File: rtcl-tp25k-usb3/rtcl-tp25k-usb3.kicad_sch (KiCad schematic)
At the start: 102 parts, among them J1 ZX360D-B-10P(30), J10 SSQ-106-02-F-D-RA, J2 0525592253, J3 BTB-DF40C-60DS-0.4V(51), J4 DF40C-60DS-0.4V(51), J5 JTAG, J6 Conn_01x02, J7 Conn_01x03, Q1 NTK3134NT1G, Q2 NTK3134NT1G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

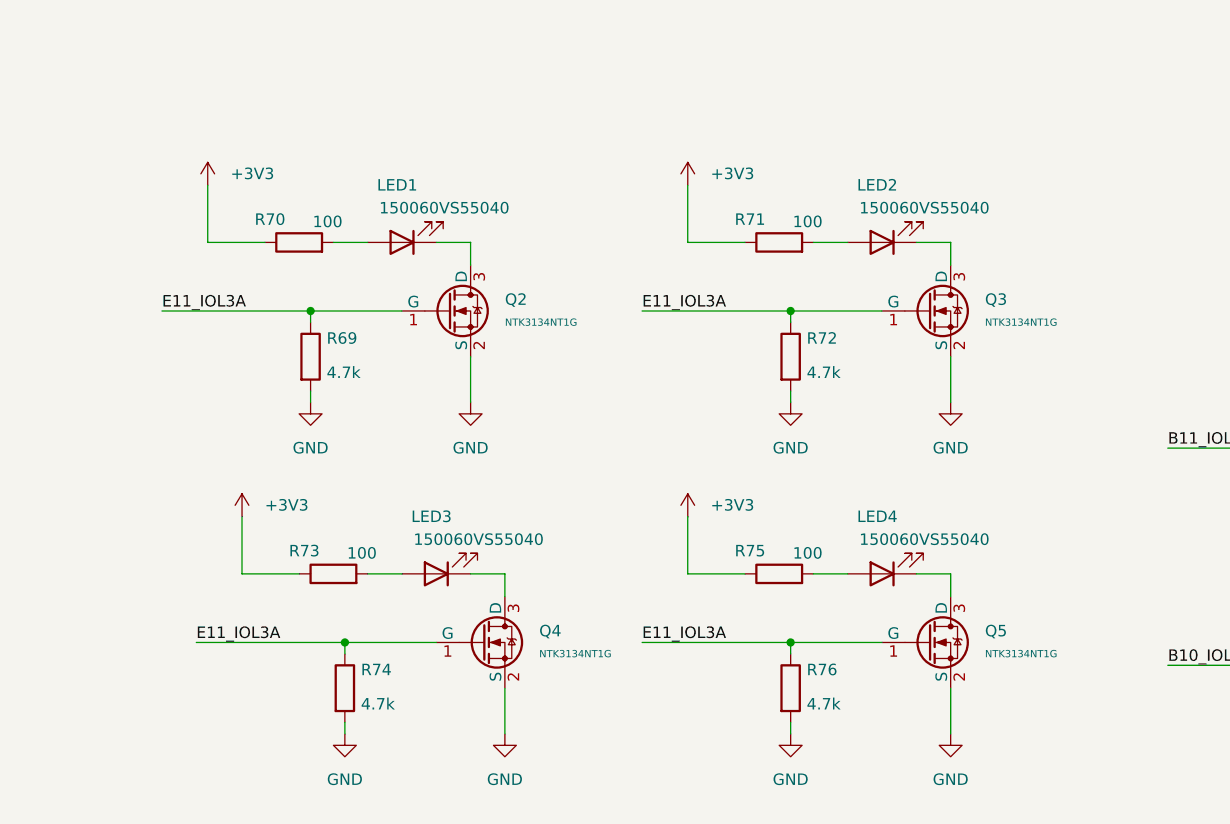
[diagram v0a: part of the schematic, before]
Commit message: Refactor KiCad project files for improved layout and organization
- Updated active layer in the project file to layer 5 for better visibility.
- Modified selection filter settings to hide dimensions, footprints, graphics, keepouts, other items, pads, tracks, vias, and zones.
- Cleared used designators in the project file to streamline component management.
- Adjusted junction and wire coordinates in the schematic for better alignment and clarity.
- Renamed labels in the schematic for consistency and clarity.
- Updated component positions and properties in the schematic to enhance layout.
- Modified footprint properties in the module file for improved design accuracy.
- Changed UUIDs for various elements to ensure uniqueness and prevent conflicts.
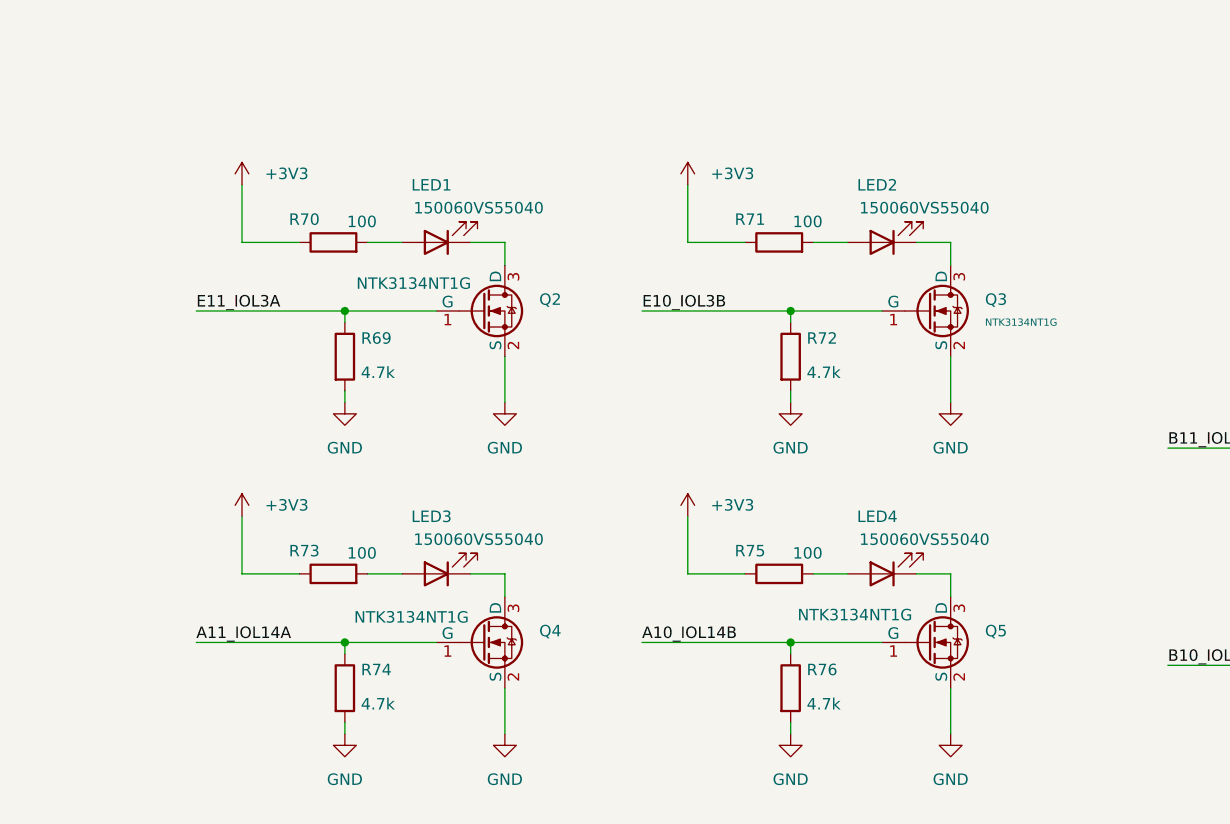
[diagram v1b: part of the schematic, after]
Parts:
- SW1, SW2, SW4: footprint (none) -> rtcl-tp25k-usb3:B3U-1100P
- SW3: footprint (none) -> rtcl-tp25k-usb3:218-2LP_CTS
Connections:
- net A10_IOL14B: now also Q5.1 (G), R76.1
- net A11_IOL14A: now also Q4.1 (G), R74.1
- net E10_IOL3B: now also Q3.1 (G), R72.1
- net E11_IOL3A: no longer Q3.1 (G), Q4.1 (G), Q5.1 (G), R72.1, R74.1, R76.1
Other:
- moved on the sheet: LED1, Q2, R69, R70

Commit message: Refactor KiCad project files: update active layer, toggle visibility settings, and remove unnecessary junctions and wires
- Changed active layer from 5 to 0 in the .kicad_prl file.
- Modified visibility settings for text, tracks, and vias in the .kicad_prl file.
- Updated visible layers string in the .kicad_prl file.
- Removed redundant junctions and wires from the .kicad_sch file to clean up the schematic.
- Added new wire connections and labels for better clarity in the .kicad_sch file.
- Adjusted positions of several labels for improved layout in the .kicad_sch file.
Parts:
- removed Q1: NTK3134NT1G, Package_TO_SOT_SMD:SOT-723, symbol PCM_JLCPCB-Transistors:NMOS,2SK3018
- removed R65: 1k, Resistor_SMD:R_0402_1005Metric, symbol Device:R
- removed R66: 4.7k, Resistor_SMD:R_0402_1005Metric, symbol Device:R
- J3: value BTB-DF40C-60DS-0.4V(51) -> DF40C(2.0)-60DS-0.4V(51)
- J4: value DF40C-60DS-0.4V(51) -> DF40C(2.0)-60DS-0.4V(51)
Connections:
- net MIPI_GPIO0 is gone; now on net A1_IOB24A_40P: J2.17 (GPIO0)
- net MIPI_GPIO1 is gone; now on net E3_IOB60A_40P: J2.18 (GPIO1)
- net A10_IOL14B: now also Q2.1 (G), R69.1; no longer Q5.1 (G), R76.1
- net A11_IOL14A: now also Q3.1 (G), R72.1; no longer Q4.1 (G), R74.1
- net B10_IOL12B: now also C11.2, R78.1; no longer C12.2, R79.1
- net B11_IOL12A: now also C12.2, R79.1; no longer C11.2, R78.1
- net E10_IOL3B: now also Q4.1 (G), R74.1; no longer Q3.1 (G), R72.1
- net E11_IOL3A: now also Q5.1 (G), R76.1; no longer Q2.1 (G), R69.1

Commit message: WIP
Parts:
- J10: footprint rtcl-p25k-usb3:PMOD_02x06_2.54mm -> rtcl-tp25k-usb3:PMOD_02x06_2.54mm
- J4: footprint rtcl-p25k-usb3:CONN_DF40C-60DS_HIR -> rtcl-tp25k-usb3:CONN_DF40C-60DS_HIR
- L1: footprint rtcl-p25k-usb3:INDC2016X100N -> rtcl-tp25k-usb3:INDC2016X100N
- RN1, RN2, RN3, RN4, RN5, RN6, RN7, RN8, RN9: footprint rtcl-p25k-usb3:RES_YC104_YAG -> rtcl-tp25k-usb3:RES_YC104_YAG
- U4: footprint rtcl-p25k-usb3:DMQ0006A -> rtcl-tp25k-usb3:DMQ0006A
- X1: footprint rtcl-p25k-usb3:XTAL_ABM8-30.000MHz-D1X-T -> rtcl-tp25k-usb3:XTAL_ABM8-30.000MHz-D1X-T
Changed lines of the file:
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@@
 			)
 		)
-		(property "Footprint" "rtcl-p25k-usb3:RES_YC104_YAG"
+		(property "Footprint" "rtcl-tp25k-usb3:RES_YC104_YAG"
 			(at 251.46 203.835 90)
 			(hide yes)
@@
 			)
 		)
-		(property "Footprint" "rtcl-p25k-usb3:RES_YC104_YAG"
+		(property "Footprint" "rtcl-tp25k-usb3:RES_YC104_YAG"
 			(at 251.46 306.705 90)
 			(hide yes)
@@
 			)
 		)
-		(property "Footprint" "rtcl-p25k-usb3:DMQ0006A"
+		(property "Footprint" "rtcl-tp25k-usb3:DMQ0006A"
 			(at 97.79 525.526 0)
 			(hide yes)
@@
 			)
 		)
-		(property "Footprint" "rtcl-p25k-usb3:RES_YC104_YAG"
+		(property "Footprint" "rtcl-tp25k-usb3:RES_YC104_YAG"
 			(at 251.46 276.225 90)
 			(hide yes)
@@
 			)
 		)
-		(property "Footprint" "rtcl-p25k-usb3:RES_YC104_YAG"
+		(property "Footprint" "rtcl-tp25k-usb3:RES_YC104_YAG"
 			(at 251.46 342.265 90)
 			(hide yes)
@@
 			)
 		)
-		(property "Footprint" "rtcl-p25k-usb3:CONN_DF40C-60DS_HIR"
+		(property "Footprint" "rtcl-tp25k-usb3:CONN_DF40C-60DS_HIR"
 			(at 486.41 278.13 0)
 			(hide yes)
@@
 			)
 		)
-		(property "Footprint" "rtcl-p25k-usb3:RES_YC104_YAG"
+		(property "Footprint" "rtcl-tp25k-usb3:RES_YC104_YAG"
 			(at 251.46 250.825 90)
 			(hide yes)
@@
 			)
 		)
-		(property "Footprint" "rtcl-p25k-usb3:RES_YC104_YAG"
+		(property "Footprint" "rtcl-tp25k-usb3:RES_YC104_YAG"
 			(at 251.46 286.385 90)
 			(hide yes)
@@
 			)
 		)
-		(property "Footprint" "rtcl-p25k-usb3:XTAL_ABM8-30.000MHz-D1X-T"
+		(property "Footprint" "rtcl-tp25k-usb3:XTAL_ABM8-30.000MHz-D1X-T"
 			(at 134.62 311.15 0)
 			(hide yes)
@@
 			)
 		)
-		(property "Footprint" "rtcl-p25k-usb3:RES_YC104_YAG"
+		(property "Footprint" "rtcl-tp25k-usb3:RES_YC104_YAG"
 			(at 251.46 316.865 90)
 			(hide yes)
@@
 			)
 		)
-		(property "Footprint" "rtcl-p25k-usb3:RES_YC104_YAG"
+		(property "Footprint" "rtcl-tp25k-usb3:RES_YC104_YAG"
 			(at 251.46 332.105 90)
 			(hide yes)
@@
 			)
 		)
-		(property "Footprint" "rtcl-p25k-usb3:RES_YC104_YAG"
+		(property "Footprint" "rtcl-tp25k-usb3:RES_YC104_YAG"
 			(at 251.46 260.985 90)
 			(hide yes)
@@
 			)
 		)
-		(property "Footprint" "rtcl-p25k-usb3:INDC2016X100N"
+		(property "Footprint" "rtcl-tp25k-usb3:INDC2016X100N"
 			(at 125.73 502.92 0)
 			(hide yes)
@@
 			)
 		)
-		(property "Footprint" "rtcl-p25k-usb3:PMOD_02x06_2.54mm"
+		(property "Footprint" "rtcl-tp25k-usb3:PMOD_02x06_2.54mm"
 			(at 488.95 415.29 0)
 			(hide yes)

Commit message: DRCは通した
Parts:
- J1: footprint rtcl-p25k-usb3:CONN10_ZX360D-B-10P30_HIR -> rtcl-tp25k-usb3:CONN10_ZX360D-B-10P30_HIR
- J2: footprint rtcl-p25k-usb3:CON_525592253_MOL -> rtcl-tp25k-usb3:CON_525592253_MOL
- J3: footprint rtcl-p25k-usb3:CONN_DF40C-60DS_HIR -> rtcl-tp25k-usb3:CONN_DF40C-60DS_HIR
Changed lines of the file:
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@@
 			)
 		)
-		(property "Footprint" "rtcl-p25k-usb3:CON_525592253_MOL"
+		(property "Footprint" "rtcl-tp25k-usb3:CON_525592253_MOL"
 			(at 176.784 390.652 0)
 			(hide yes)
@@
 			)
 		)
-		(property "Footprint" "rtcl-p25k-usb3:CONN_DF40C-60DS_HIR"
+		(property "Footprint" "rtcl-tp25k-usb3:CONN_DF40C-60DS_HIR"
 			(at 383.54 278.13 0)
 			(hide yes)
@@
 			)
 		)
-		(property "Footprint" "rtcl-p25k-usb3:CONN10_ZX360D-B-10P30_HIR"
+		(property "Footprint" "rtcl-tp25k-usb3:CONN10_ZX360D-B-10P30_HIR"
 			(at 52.07 186.69 0)
 			(hide yes)

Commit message: PMOD配線長調整
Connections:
- net VCCIO33 is gone; now on net +3V3: C77.1, J10.11 (Pin_11), J10.12 (Pin_12)
- no-connect marks 0 -> 1
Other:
- moved on the sheet: C1, C10, C11, C12, C15, C16, C17, C18, C19, C2, C20, C21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

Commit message: WIP
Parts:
- added R81: 4.7k, Resistor_SMD:R_0402_1005Metric, symbol Device:R
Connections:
- net A1_IOB24A_40P: now also R81.1
- net GND: now also R81.2
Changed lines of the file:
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@@
 	)
 	(junction
+		(at 337.82 86.36)
+		(diameter 0)
+		(color 0 0 0 0)
+	)
+	(junction
 		(at 279.4 80.01)
 		(diameter 0)
@@
 	(wire
 		(pts
-			(xy 339.09 86.36) (xy 339.09 69.85)
+			(xy 342.9 86.36) (xy 342.9 69.85)
 		)
 		(stroke
@@
 	(wire
 		(pts
+			(xy 337.82 99.06) (xy 337.82 100.33)
+		)
+		(stroke
+			(width 0)
+			(type default)
+		)
+	)
+	(wire
+		(pts
 			(xy 82.55 240.03) (xy 82.55 241.3)
 		)
@@
 	(wire
 		(pts
+			(xy 337.82 86.36) (xy 337.82 91.44)
+		)
+		(stroke
+			(width 0)
+			(type default)
+		)
+	)
+	(wire
+		(pts
 			(xy 217.17 111.76) (xy 194.31 111.76)
 		)
@@
 	(wire
 		(pts
-			(xy 321.31 88.9) (xy 341.63 88.9)
+			(xy 321.31 88.9) (xy 345.44 88.9)
 		)
 		(stroke
@@
 	(wire
 		(pts
+			(xy 337.82 86.36) (xy 342.9 86.36)
+		)
+		(stroke
+			(width 0)
+			(type default)
+		)
+	)
+	(wire
+		(pts
 			(xy 288.29 80.01) (xy 279.4 80.01)
 		)
@@
 	(wire
 		(pts
-			(xy 341.63 72.39) (xy 372.11 72.39)
+			(xy 345.44 72.39) (xy 372.11 72.39)
 		)
 		(stroke
@@
 	(wire
 		(pts
-			(xy 339.09 69.85) (xy 372.11 69.85)
+			(xy 342.9 69.85) (xy 372.11 69.85)
 		)
 		(stroke
@@
 	(wire
 		(pts
-			(xy 321.31 86.36) (xy 339.09 86.36)
+			(xy 321.31 86.36) (xy 337.82 86.36)
 		)
 		(stroke
@@
 	(wire
 		(pts
-			(xy 341.63 72.39) (xy 341.63 88.9)
+			(xy 345.44 72.39) (xy 345.44 88.9)
 		)
 		(stroke
@@
 	)
 	(symbol
+		(lib_id "Device:R")
+		(at 337.82 95.25 0)
+		(unit 1)
+		(body_style 1)
+		(exclude_from_sim no)
+		(in_bom yes)
+		(on_board yes)
+		(in_pos_files yes)
+		(dnp no)
+		(property "Reference" "R81"
+			(at 339.598 93.218 0)
+			(show_name no)
+			(do_not_autoplace no)
+			(effects
+				(font
+					(size 1.27 1.27)
+				)
+				(justify left)
+			)
+		)
+		(property "Value" "4.7k"
+			(at 339.598 97.028 0)
+			(show_name no)
+			(do_not_autoplace no)
+			(effects
+				(font
+					(size 1.27 1.27)
+				)
+				(justify left)
+			)
+		)
+		(property "Footprint" "Resistor_SMD:R_0402_1005Metric"
+			(at 336.042 95.25 90)
+			(hide yes)
+			(show_name no)
+			(do_not_autoplace no)
+			(effects
+				(font
+					(size 1.27 1.27)
+				)
+			)
+		)
+		(property "Datasheet" ""
+			(at 337.82 95.25 0)
+			(hide yes)
+			(show_name no)
+			(do_not_autoplace no)
+			(effects
+				(font
+					(size 1.27 1.27)
+				)
+			)
+		)
+		(property "Description" "Resistor"
+			(at 337.82 95.25 0)
+			(hide yes)
+			(show_name no)
+			(do_not_autoplace no)
+			(effects
+				(font
+					(size 1.27 1.27)
+				)
+			)
+		)
+		(pin "1"
+		)
+		(pin "2"
+		)
+		(instances
+			(project "rtcl-tp25k-usb3"
+				(path "/3111823c-3b86-4a35-a2d4-382a0824eec6"
+					(reference "R81")
+					(unit 1)
+				)
+			)
+		)
+	)
+	(symbol
 		(lib_id "Device:R_Pack04")
 		(at 189.23 137.16 270)
@@
 					(unit 1)
 				)
+			)
+		)
+	)
+	(symbol
+		(lib_id "power:GND")
+		(at 337.82 100.33 0)
+		(unit 1)
+		(body_style 1)
+		(exclude_from_sim no)
+		(in_bom yes)
+		(on_board yes)
+		(in_pos_files yes)
+		(dnp no)
+		(property "Reference" "#PWR0111"
+			(at 337.82 106.68 0)
+			(hide yes)
+			(show_name no)
+			(do_not_autoplace no)
+			(effects
+				(font
+					(size 1.27 1.27)
+				)
+			)
+		)
+		(property "Value" "GND"
+			(at 341.63 102.362 0)
+			(show_name no)
+			(do_not_autoplace no)
+			(effects
+				(font
+					(size 1.27 1.27)
+				)
+			)
+		)
+		(property "Footprint" ""
+			(at 337.82 100.33 0)
+			(hide yes)
+			(show_name no)
+			(do_not_autoplace no)
+			(effects
+				(font
+					(size 1.27 1.27)
+				)
+			)
+		)
+		(property "Datasheet" ""
+			(at 337.82 100.33 0)
+			(hide yes)
+			(show_name no)
+			(do_not_autoplace no)
+			(effects
+				(font
+					(size 1.27 1.27)
+				)
+			)
+		)
+		(property "Description" "Power symbol creates a global label with name \"GND\" , ground"
+			(at 337.82 100.33 0)
+			(hide yes)
+			(show_name no)
+			(do_not_autoplace no)
+			(effects
+				(font
+					(size 1.27 1.27)
+				)
+			)
+		)
+		(pin "1"
+		)
+		(instances
+			(project "rtcl-tp25k-usb3"
+				(path "/3111823c-3b86-4a35-a2d4-382a0824eec6"
+					(reference "#PWR0111")
+					(unit 1)
+				)

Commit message: WIP
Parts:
- added C75, C76: 0.1uF, Capacitor_SMD:C_0402_1005Metric, symbol Device:C
- added Q6: NTK3134NT1G, Package_TO_SOT_SMD:SOT-723, symbol PCM_JLCPCB-Transistors:NMOS,2SK3018
- added R82: 4.7k, Resistor_SMD:R_0402_1005Metric, symbol Device:R
- J10: LCSC (none) -> C37208
- J2: value 0525592253 -> CF20221V0R0-NH; LCSC (none) -> C3169524
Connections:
- net +3.3VP: now also C75.1; no longer R63.1, R64.1
- net +5V: now also R82.1
- net G10_IOT7B: now also R68.2, Q6.1 (G); no longer R68.1, U4.1 (EN)
- net GND: now also C75.2, C76.2, Q6.2 (S); no longer R68.2
- net VCC: now also R63.1, R64.1, R68.1
- net at R62.2, U5.7 (VREF2), U5.8 (EN): now also C76.1
- new net: Q6.3 (D), R82.2, U4.1 (EN)
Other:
- moved on the sheet: C71, LED3, LED4, Q4, Q5, R57, R58, R68, R73, R74, R75, R76

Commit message: WIP
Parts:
- removed J2: CF20221V0R0-NH, rtcl-tp25k-usb3:CON_525592253_MOL, symbol rtcl-xcaup-usb3:RASPPICAM22
- added J2: CF20221V0R0-NH, rtcl-tp25k-usb3:CON_525592253_MOL, symbol rtcl-tp25k-usb3:RASPPICAM22
- added R83: 4.7k, Resistor_SMD:R_0402_1005Metric, symbol Device:R
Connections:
- net +3.3VP: now also J2.22 (3V3)
- net A1_IOB24A_40P: now also J2.17 (GPIO0)
- net E3_IOB60A_40P: now also J2.18 (GPIO1), R83.1
- net GND: now also J2.1 (GND), J2.10 (GND), J2.13 (GND), J2.16 (GND), J2.19 (GND), J2.4 (GND), J2.7 (GND), R83.2
- net M0_CK_N: now also J2.8 (CN)
- net M0_CK_P: now also J2.9 (CP)
- net M0_D0_N: now also J2.2 (DN0)
- net M0_D0_P: now also J2.3 (DP0)
- net M0_D1_N: now also J2.5 (DN1)
- net M0_D1_P: now also J2.6 (DP1)
- net M0_D2_N: now also J2.11 (DN2)
- net M0_D2_P: now also J2.12 (DP2)
- net M0_D3_N: now also J2.14 (DN3)
- net M0_D3_P: now also J2.15 (DP3)
- net MIPI_SCL: now also J2.20 (SCL)
- net MIPI_SDA: now also J2.21 (SDA)
